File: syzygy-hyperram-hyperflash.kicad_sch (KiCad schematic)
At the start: 31 parts, among them IC1 ATTINY44A-MMH, IC2 TLV6710DDCT, IC3 S27KL0641DABHI020, IC4 S71KL256SC0BHI, J1 SYZYGY_STD, J2 Conn_02x03_Odd_Even, J3 Conn_02x03_Odd_Even

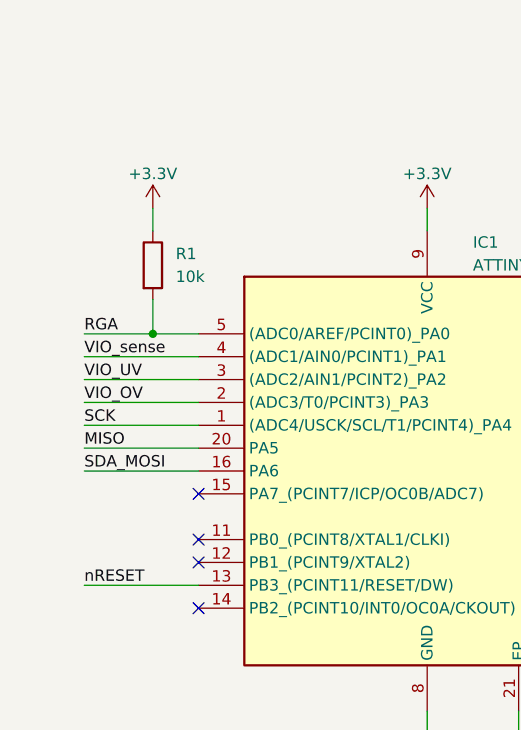
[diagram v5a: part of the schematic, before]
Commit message: Removed unnecessary holes to make pcb smaller. Rearranged signals connected to ATTiny.
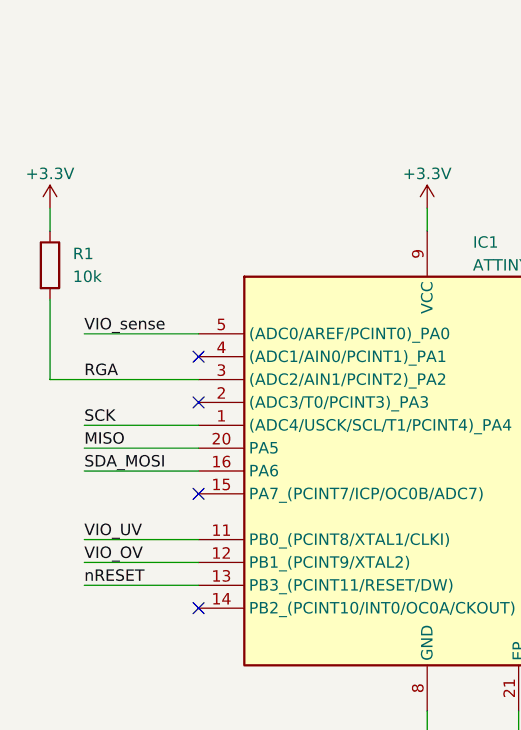
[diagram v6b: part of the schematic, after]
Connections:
- net RGA: now also IC1.3 ((ADC2/AIN1/PCINT2)_PA2); no longer IC1.5 ((ADC0/AREF/PCINT0)_PA0)
- net VIO_OV: now also IC1.12 (PB1_(PCINT9/XTAL2)); no longer IC1.2 ((ADC3/T0/PCINT3)_PA3)
- net VIO_UV: now also IC1.11 (PB0_(PCINT8/XTAL1/CLKI)); no longer IC1.3 ((ADC2/AIN1/PCINT2)_PA2)
- net VIO_sense: now also IC1.5 ((ADC0/AREF/PCINT0)_PA0); no longer IC1.4 ((ADC1/AIN0/PCINT1)_PA1)
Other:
- moved on the sheet: R1
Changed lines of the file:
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@@
 	)
 	(junction
-		(at 45.72 135.89)
-		(diameter 0)
-		(color 0 0 0 0)
-	)
-	(junction
 		(at 217.17 78.74)
 		(diameter 0)
@@
 	)
 	(no_connect
-		(at 50.8 161.29)
+		(at 50.8 138.43)
 	)
 	(no_connect
-		(at 50.8 158.75)
+		(at 50.8 143.51)
 	)
 	(no_connect
@@
 	(wire
 		(pts
-			(xy 38.1 138.43) (xy 50.8 138.43)
-		)
-		(stroke
-			(width 0)
-			(type default)
-		)
-	)
-	(wire
-		(pts
 			(xy 114.3 121.92) (xy 114.3 124.46)
 		)
@@
 	(wire
 		(pts
-			(xy 38.1 135.89) (xy 45.72 135.89)
+			(xy 38.1 135.89) (xy 50.8 135.89)
 		)
 		(stroke
@@
 	(wire
 		(pts
-			(xy 38.1 140.97) (xy 50.8 140.97)
+			(xy 38.1 158.75) (xy 50.8 158.75)
 		)
 		(stroke
@@
 	(wire
 		(pts
-			(xy 38.1 143.51) (xy 50.8 143.51)
+			(xy 34.29 132.08) (xy 34.29 140.97)
+		)
+		(stroke
+			(width 0)
+			(type default)
+		)
+	)
+	(wire
+		(pts
+			(xy 38.1 161.29) (xy 50.8 161.29)
 		)
 		(stroke
@@
 	(wire
 		(pts
+			(xy 34.29 140.97) (xy 50.8 140.97)
+		)
+		(stroke
+			(width 0)
+			(type default)
+		)
+	)
+	(wire
+		(pts
 			(xy 110.49 156.21) (xy 120.65 156.21)
 		)
@@
 	(wire
 		(pts
-			(xy 45.72 135.89) (xy 50.8 135.89)
-		)
-		(stroke
-			(width 0)
-			(type default)
-		)
-	)
-	(wire
-		(pts
 			(xy 189.23 152.4) (xy 199.39 152.4)
 		)
@@
 	(wire
 		(pts
-			(xy 45.72 132.08) (xy 45.72 135.89)
-		)
-		(stroke
-			(width 0)
-			(type default)
-		)
-	)
-	(wire
-		(pts
 			(xy 50.8 63.5) (xy 62.23 63.5)
 		)
@@
 	(wire
 		(pts
-			(xy 45.72 121.92) (xy 45.72 124.46)
+			(xy 34.29 121.92) (xy 34.29 124.46)
 		)
 		(stroke
@@
 	)
 	(label "VIO_sense"
-		(at 38.1 138.43 0)
+		(at 38.1 135.89 0)
 		(fields_autoplaced yes)
 		(effects
@@
 	)
 	(label "VIO_UV"
-		(at 38.1 140.97 0)
+		(at 38.1 158.75 0)
 		(fields_autoplaced yes)
 		(effects
@@
 	)
 	(label "VIO_OV"
-		(at 38.1 143.51 0)
+		(at 38.1 161.29 0)
 		(fields_autoplaced yes)
 		(effects
@@
 	)
 	(label "RGA"
-		(at 38.1 135.89 0)
+		(at 38.1 140.97 0)
 		(fields_autoplaced yes)
 		(effects
@@
 	(symbol
 		(lib_id "power:+3.3V")
-		(at 45.72 121.92 0)
+		(at 34.29 121.92 0)
 		(unit 1)
 		(exclude_from_sim no)
@@
 		(dnp no)
 		(property "Reference" "#PWR03"
-			(at 45.72 125.73 0)
+			(at 34.29 125.73 0)
 			(effects
 				(font
@@
 		)
 		(property "Value" "+3.3V"
-			(at 45.72 118.11 0)
+			(at 34.29 118.11 0)
 			(effects
 				(font
@@
 		)
 		(property "Footprint" ""
-			(at 45.72 121.92 0)
+			(at 34.29 121.92 0)
 			(effects
 				(font
@@
 		)
 		(property "Datasheet" ""
-			(at 45.72 121.92 0)
+			(at 34.29 121.92 0)
 			(effects
 				(font
@@
 		)
 		(property "Description" "Power symbol creates a global label with name \"+3.3V\""
-			(at 45.72 121.92 0)
+			(at 34.29 121.92 0)
 			(effects
 				(font
@@
 	(symbol
 		(lib_id "Device:R")
-		(at 45.72 128.27 0)
+		(at 34.29 128.27 0)
 		(unit 1)
 		(exclude_from_sim no)
@@
 		(fields_autoplaced yes)
 		(property "Reference" "R1"
-			(at 48.26 126.9999 0)
+			(at 36.83 126.9999 0)
 			(effects
 				(font
@@
 		)
 		(property "Value" "10k"
-			(at 48.26 129.5399 0)
+			(at 36.83 129.5399 0)
 			(effects
 				(font
@@
 		)
 		(property "Footprint" "Resistor_SMD:R_0603_1608Metric_Pad0.98x0.95mm_HandSolder"
-			(at 43.942 128.27 90)
+			(at 32.512 128.27 90)
 			(effects
 				(font
@@
 		)
 		(property "Datasheet" "~"
-			(at 45.72 128.27 0)
+			(at 34.29 128.27 0)
 			(effects
 				(font
@@
 		)
 		(property "Description" "Resistor"
-			(at 45.72 128.27 0)
+			(at 34.29 128.27 0)
 			(effects
 				(font
